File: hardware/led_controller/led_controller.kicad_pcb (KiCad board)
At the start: 2 copper layers, 50 x 70 mm, 31 parts, among them J1 Header, J2 Header, J3 Header, J4 Header, J5 POWER, J6 Conn_01x02, U1 74AHCT125, U3 Waveshare ESP32-S3/C6 Zero

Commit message: Updated footprint
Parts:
- J6: footprint TerminalBlock_Phoenix:TerminalBlock_Phoenix_MPT-0,5-2-2.54_1x02_P2.54mm_Horizontal -> TerminalBlock:TerminalBlock_Xinya_XY308-2.54-2P_1x02_P2.54mm_Horizontal
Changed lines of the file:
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@@
 		)
 	)
-	(footprint "TerminalBlock_Phoenix:TerminalBlock_Phoenix_MPT-0,5-2-2.54_1x02_P2.54mm_Horizontal"
+	(footprint "TerminalBlock:TerminalBlock_Xinya_XY308-2.54-2P_1x02_P2.54mm_Horizontal"
 		(layer "F.Cu")
 		(at 162.2175 95.975 90)
-		(descr "Terminal Block Phoenix MPT-0,5-2-2.54, 2 pins, pitch 2.54mm, size 5.54x6.2mm, drill diameter 1.1mm, pad diameter 2.2mm, http://www.mouser.com/ds/2/324/ItemDetail_1725656-920552.pdf")
-		(tags "THT Terminal Block Phoenix MPT-0,5-2-2.54 pitch 2.54mm size 5.54x6.2mm drill 1.1mm pad 2.2mm")
+		(descr "Terminal Block Xinya XY308-2.54-2P, 2 pins, pitch 2.54mm, size 5.58x6.5mm, drill diameter 1.2mm, pad diameter 2mm, http://www.xinyaelectronic.com/product/xy308-254")
+		(tags "THT Terminal Block Xinya XY308-2.54-2P pitch 2.54mm size 5.58x6.5mm drill 1.2mm pad 2mm")
 		(property "Reference" "J6"
-			(at -3.025 -0.0175 180)
+			(at -2.925 0.1825 180)
 			(layer "F.SilkS")
 			(effects
@@
 		)
 		(property "Value" "Conn_01x02"
-			(at 1.27 4.22 90)
+			(at 1.27 4.52 90)
 			(layer "F.Fab")
 			(effects
@@
 		(duplicate_pad_numbers_are_jumpers no)
 		(fp_line
-			(start 4.16 -3.22)
-			(end 4.16 3.22)
+			(start 4.18 -3.22)
+			(end 4.18 3.52)
 			(stroke
 				(width 0.12)
@@
 		)
 		(fp_line
-			(start -1.62 -3.22)
-			(end 4.16 -3.22)
+			(start -1.64 -3.22)
+			(end 4.18 -3.22)
 			(stroke
 				(width 0.12)
@@
 		)
 		(fp_line
-			(start -1.62 -2.7)
-			(end 4.16 -2.7)
+			(start -1.64 -1.5)
+			(end 4.18 -1.5)
 			(stroke
 				(width 0.12)
@@
 		)
 		(fp_line
-			(start 3.57 2.6)
-			(end 4.16 2.6)
+			(start -1.64 1.6)
+			(end 4.18 1.6)
 			(stroke
 				(width 0.12)
@@
 		)
 		(fp_line
-			(start 1.03 2.6)
-			(end 1.51 2.6)
+			(start -1.64 2.6)
+			(end 4.18 2.6)
 			(stroke
 				(width 0.12)
@@
 		)
 		(fp_line
-			(start -1.62 2.6)
-			(end -1.03 2.6)
+			(start 4.18 3.52)
+			(end 0.3 3.52)
 			(stroke
 				(width 0.12)
@@
 		)
 		(fp_line
-			(start 4.16 3.22)
-			(end 3.57 3.22)
+			(start -0.3 3.52)
+			(end -1.64 3.52)
 			(stroke
 				(width 0.12)
@@
 		)
 		(fp_line
-			(start 1.51 3.22)
-			(end 1.03 3.22)
-			(stroke
-				(width 0.12)
-				(type solid)
-			)
-			(layer "F.SilkS")
-		)
-		(fp_line
-			(start -1.03 3.22)
-			(end -1.62 3.22)
-			(stroke
-				(width 0.12)
-				(type solid)
-			)
-			(layer "F.SilkS")
-		)
-		(fp_line
-			(start -1.62 3.22)
-			(end -1.62 -3.22)
+			(start -1.64 3.52)
+			(end -1.64 -3.22)
 			(stroke
 				(width 0.12)
@@
 		(fp_poly
 			(pts
-				(xy 0 3.57) (xy 0.44 4.18) (xy -0.44 4.18)
+				(xy 0 3.52) (xy 0.44 4.13) (xy -0.44 4.13)
 			)
 			(stroke
@@
 		)
 		(fp_rect
-			(start -2 -3.6)
-			(end 4.54 3.6)
+			(start -2.02 -3.6)
+			(end 4.57 3.9)
 			(stroke
 				(width 0.05)
@@
 		)
 		(fp_line
-			(start 4.04 -3.1)
-			(end 4.04 3.1)
+			(start 4.06 -3.1)
+			(end 4.06 3.4)
 			(stroke
 				(width 0.1)
@@
 		)
 		(fp_line
-			(start -1.5 -3.1)
-			(end 4.04 -3.1)
+			(start -1.52 -3.1)
+			(end 4.06 -3.1)
 			(stroke
 				(width 0.1)
@@
 		)
 		(fp_line
-			(start -1.5 -2.7)
-			(end 4.04 -2.7)
+			(start -1.52 -1.5)
+			(end 4.06 -1.5)
 			(stroke
 				(width 0.1)
@@
 		)
 		(fp_line
-			(start 3.24 -0.834)
-			(end 1.706 0.7)
+			(start 3.176 -0.758)
+			(end 1.782 0.636)
 			(stroke
 				(width 0.1)
@@
 		)
 		(fp_line
-			(start 0.7 -0.834)
-			(end -0.834 0.7)
+			(start 0.636 -0.758)
+			(end -0.758 0.636)
 			(stroke
 				(width 0.1)
@@
 		)
 		(fp_line
-			(start 3.374 -0.7)
-			(end 1.84 0.834)
+			(start 3.298 -0.636)
+			(end 1.904 0.758)
 			(stroke
 				(width 0.1)
@@
 		)
 		(fp_line
-			(start 0.834 -0.7)
-			(end -0.7 0.834)
+			(start 0.758 -0.636)
+			(end -0.636 0.758)
 			(stroke
 				(width 0.1)
@@
 		)
 		(fp_line
-			(start -1.5 2.6)
-			(end -1.5 -3.1)
+			(start -1.52 1.6)
+			(end 4.06 1.6)
 			(stroke
 				(width 0.1)
@@
 		)
 		(fp_line
-			(start -1.5 2.6)
-			(end 4.04 2.6)
+			(start -1.52 2.6)
+			(end -1.52 -3.1)
 			(stroke
 				(width 0.1)
@@
 		)
 		(fp_line
-			(start 4.04 3.1)
-			(end -1 3.1)
+			(start -1.52 2.6)
+			(end 4.06 2.6)
 			(stroke
 				(width 0.1)
@@
 		)
 		(fp_line
-			(start -1 3.1)
-			(end -1.5 2.6)
+			(start 4.06 3.4)
+			(end -0.72 3.4)
+			(stroke
+				(width 0.1)
+				(type solid)
+			)
+			(layer "F.Fab")
+		)
+		(fp_line
+			(start -0.72 3.4)
+			(end -1.52 2.6)
 			(stroke
 				(width 0.1)
@@
 		(fp_circle
 			(center 2.54 0)
-			(end 3.64 0)
+			(end 3.54 0)
 			(stroke
 				(width 0.1)
@@
 		(fp_circle
 			(center 0 0)
-			(end 1.1 0)
+			(end 1 0)
 			(stroke
 				(width 0.1)
@@
 		)
 		(fp_text user "${REFERENCE}"
-			(at 1.27 2 90)
+			(at 1.27 2.15 90)
 			(layer "F.Fab")
 			(effects
@@
 			)
 		)
-		(pad "" np_thru_hole circle
-			(at 0 2.54 90)
-			(size 1.1 1.1)
-			(drill 1.1)
-			(layers "*.Cu" "*.Mask")
-		)
-		(pad "" np_thru_hole circle
-			(at 2.54 2.54 90)
-			(size 1.1 1.1)
-			(drill 1.1)
-			(layers "*.Cu" "*.Mask")
-		)
 		(pad "1" thru_hole roundrect
 			(at 0 0 90)
-			(size 2.2 2.2)
-			(drill 1.1)
+			(size 2 2)
+			(drill 1.2)
 			(layers "*.Cu" "*.Mask")
 			(remove_unused_layers no)
-			(roundrect_rratio 0.113636)
+			(roundrect_rratio 0.125)
 			(net "GND")
 			(pinfunction "Pin_1_1")
@@
 		(pad "2" thru_hole circle
 			(at 2.54 0 90)
-			(size 2.2 2.2)
-			(drill 1.1)
+			(size 2 2)
+			(drill 1.2)
 			(layers "*.Cu" "*.Mask")
 			(remove_unused_layers no)
@@
 		)
 		(embedded_fonts no)
-		(model "${KICAD10_3DMODEL_DIR}/TerminalBlock_Phoenix.3dshapes/TerminalBlock_Phoenix_MPT-0,5-2-2.54_1x02_P2.54mm_Horizontal.step"
+		(model "${KICAD10_3DMODEL_DIR}/TerminalBlock.3dshapes/TerminalBlock_Xinya_XY308-2.54-2P_1x02_P2.54mm_Horizontal.step"
 			(offset
 				(xyz 0 0 0)
@@
 		(tags "capacitor handsolder")
 		(property "Reference" "C9"
-			(at 0 -1.85 0)
+			(at -0.2 1.9 0)
 			(layer "F.SilkS")
 			(effects

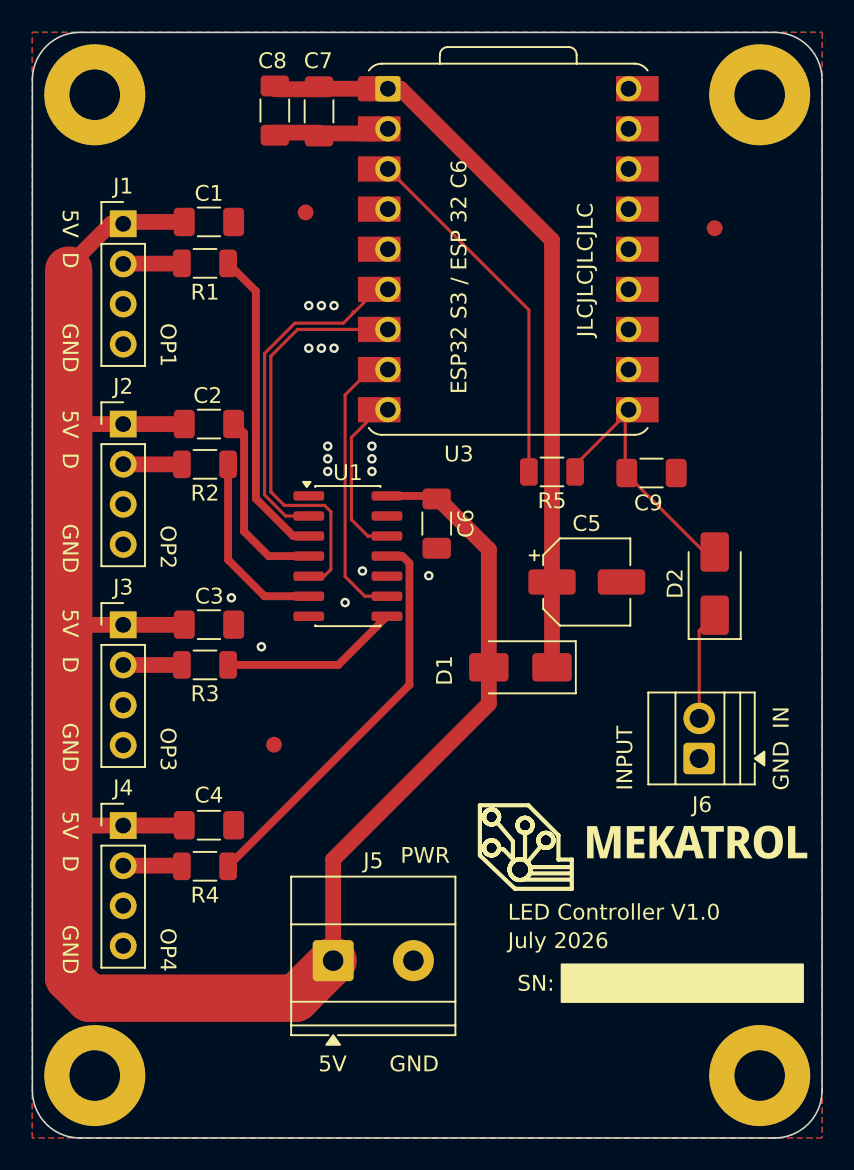
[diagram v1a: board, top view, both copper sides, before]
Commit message: Update hole layout
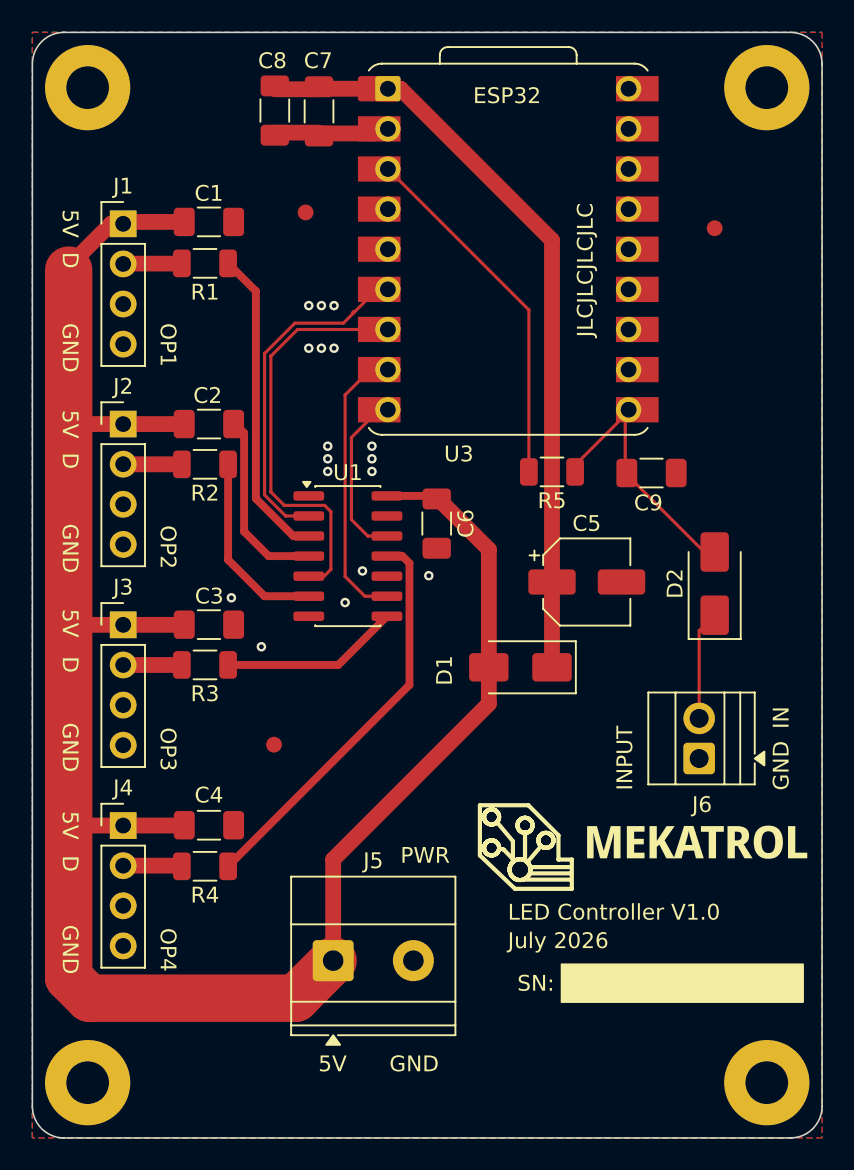
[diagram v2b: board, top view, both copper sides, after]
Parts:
- H1, H2, H3, H4: footprint MountingHole:MountingHole_3.2mm_M3_Pad -> MountingHole:MountingHole_2.7mm_M2.5_Pad
- moved H1 0.64 mm to (123.5, 53.5)
- moved H3 0.64 mm to (123.5, 116.5)
- moved H2 0.64 mm to (166.5, 53.5)
- moved H4 0.64 mm to (166.5, 116.5)
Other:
- outline, holes or cut-outs redrawn
- board text added: "ESP32"
- board text removed: "ESP32 S3 / ESP 32 C6"
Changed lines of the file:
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@@
 		)
 	)
-	(footprint "MountingHole:MountingHole_3.2mm_M3_Pad"
+	(footprint "MountingHole:MountingHole_2.7mm_M2.5_Pad"
 		(layer "F.Cu")
-		(at 166.05 116.05)
-		(descr "Mounting Hole 3.2mm, M3, generated by kicad-footprint-generator mountinghole.py")
-		(tags "mountinghole M3")
+		(at 166.5 116.5)
+		(descr "Mounting Hole 2.7mm, M2.5, generated by kicad-footprint-generator mountinghole.py")
+		(tags "mountinghole M2.5")
 		(property "Reference" "H4"
-			(at 0 -4.15 0)
+			(at 0 -3.65 0)
 			(layer "F.SilkS")
 			(hide yes)
@@
 		)
 		(property "Value" "MountingHole_Pad"
-			(at 0 4.15 0)
+			(at 0 3.65 0)
 			(layer "F.Fab")
 			(hide yes)
@@
 		(fp_circle
 			(center 0 0)
-			(end 3.2 0)
+			(end 2.7 0)
 			(stroke
 				(width 0.15)
@@
 		(fp_circle
 			(center 0 0)
-			(end 3.45 0)
+			(end 2.95 0)
 			(stroke
 				(width 0.05)
@@
 		(pad "1" thru_hole circle
 			(at 0 0)
-			(size 6.4 6.4)
-			(drill 3.2)
+			(size 5.4 5.4)
+			(drill 2.7)
 			(layers "*.Cu" "*.Mask")
 			(remove_unused_layers no)
@@
 		)
 	)
-	(footprint "MountingHole:MountingHole_3.2mm_M3_Pad"
+	(footprint "MountingHole:MountingHole_2.7mm_M2.5_Pad"
 		(layer "F.Cu")
-		(at 166.05 53.95)
-		(descr "Mounting Hole 3.2mm, M3, generated by kicad-footprint-generator mountinghole.py")
-		(tags "mountinghole M3")
+		(at 166.5 53.5)
+		(descr "Mounting Hole 2.7mm, M2.5, generated by kicad-footprint-generator mountinghole.py")
+		(tags "mountinghole M2.5")
 		(property "Reference" "H2"
-			(at 0 -4.15 0)
+			(at 0 -3.65 0)
 			(layer "F.SilkS")
 			(hide yes)
@@
 		)
 		(property "Value" "MountingHole_Pad"
-			(at 0 4.15 0)
+			(at 0 3.65 0)
 			(layer "F.Fab")
 			(hide yes)
@@
 		(fp_circle
 			(center 0 0)
-			(end 3.2 0)
+			(end 2.7 0)
 			(stroke
 				(width 0.15)
@@
 		(fp_circle
 			(center 0 0)
-			(end 3.45 0)
+			(end 2.95 0)
 			(stroke
 				(width 0.05)
@@
 		(pad "1" thru_hole circle
 			(at 0 0)
-			(size 6.4 6.4)
-			(drill 3.2)
+			(size 5.4 5.4)
+			(drill 2.7)
 			(layers "*.Cu" "*.Mask")
 			(remove_unused_layers no)
@@
 		)
 	)
-	(footprint "MountingHole:MountingHole_3.2mm_M3_Pad"
+	(footprint "MountingHole:MountingHole_2.7mm_M2.5_Pad"
 		(layer "F.Cu")
-		(at 123.95 53.95)
-		(descr "Mounting Hole 3.2mm, M3, generated by kicad-footprint-generator mountinghole.py")
-		(tags "mountinghole M3")
+		(at 123.5 53.5)
+		(descr "Mounting Hole 2.7mm, M2.5, generated by kicad-footprint-generator mountinghole.py")
+		(tags "mountinghole M2.5")
 		(property "Reference" "H1"
-			(at 4.65 0.05 0)
+			(at 0 -3.65 0)
 			(layer "F.SilkS")
 			(hide yes)
@@
 		)
 		(property "Value" "MountingHole_Pad"
-			(at 0 4.15 0)
+			(at 0 3.65 0)
 			(layer "F.Fab")
 			(hide yes)
@@
 		(fp_circle
 			(center 0 0)
-			(end 3.2 0)
+			(end 2.7 0)
 			(stroke
 				(width 0.15)
@@
 		(fp_circle
 			(center 0 0)
-			(end 3.45 0)
+			(end 2.95 0)
 			(stroke
 				(width 0.05)
@@
 		(pad "1" thru_hole circle
 			(at 0 0)
-			(size 6.4 6.4)
-			(drill 3.2)
+			(size 5.4 5.4)
+			(drill 2.7)
 			(layers "*.Cu" "*.Mask")
 			(remove_unused_layers no)
@@
 		(embedded_fonts no)
 	)
-	(footprint "MountingHole:MountingHole_3.2mm_M3_Pad"
+	(footprint "MountingHole:MountingHole_2.7mm_M2.5_Pad"
 		(layer "F.Cu")
-		(at 123.95 116.05)
-		(descr "Mounting Hole 3.2mm, M3, generated by kicad-footprint-generator mountinghole.py")
-		(tags "mountinghole M3")
+		(at 123.5 116.5)
+		(descr "Mounting Hole 2.7mm, M2.5, generated by kicad-footprint-generator mountinghole.py")
+		(tags "mountinghole M2.5")
 		(property "Reference" "H3"
-			(at 0 -4.15 0)
+			(at 0 -3.65 0)
 			(layer "F.SilkS")
 			(hide yes)
@@
 		)
 		(property "Value" "MountingHole_Pad"
-			(at 0 4.15 0)
+			(at 0 3.65 0)
 			(layer "F.Fab")
 			(hide yes)
@@
 		(fp_circle
 			(center 0 0)
-			(end 3.2 0)
+			(end 2.7 0)
 			(stroke
 				(width 0.15)
@@
 		(fp_circle
 			(center 0 0)
-			(end 3.45 0)
+			(end 2.95 0)
 			(stroke
 				(width 0.05)
@@
 		(pad "1" thru_hole circle
 			(at 0 0)
-			(size 6.4 6.4)
-			(drill 3.2)
+			(size 5.4 5.4)
+			(drill 2.7)
 			(layers "*.Cu" "*.Mask")
 			(remove_unused_layers no)
@@
 	)
 	(gr_arc
-		(start 120 53)
-		(mid 120.878679 50.878679)
-		(end 123 50)
+		(start 120 52)
+		(mid 120.585786 50.585786)
+		(end 122 50)
 		(stroke
 			(width 0.1)
@@
 	)
 	(gr_line
-		(start 120 117)
-		(end 120 53)
+		(start 120 118)
+		(end 120 52)
 		(stroke
 			(width 0.1)
@@
 	)
 	(gr_line
-		(start 123 50)
-		(end 167 50)
+		(start 122 50)
+		(end 168 50)
 		(stroke
 			(width 0.1)
@@
 	)
 	(gr_arc
-		(start 123 120)
-		(mid 120.878679 119.12132)
-		(end 120 117)
+		(start 122 120)
+		(mid 120.585786 119.414213)
+		(end 120 118)
 		(stroke
 			(width 0.1)
@@
 	)
 	(gr_arc
-		(start 167 50)
-		(mid 169.12132 50.878679)
-		(end 170 53)
+		(start 168 50)
+		(mid 169.414213 50.585786)
+		(end 170 52)
 		(stroke
 			(width 0.1)
@@
 	)
 	(gr_line
-		(start 167 120)
-		(end 123 120)
+		(start 168 120)
+		(end 122 120)
 		(stroke
 			(width 0.1)
@@
 	)
 	(gr_line
-		(start 170 53)
-		(end 170 117)
+		(start 170 52)
+		(end 170 118)
 		(stroke
 			(width 0.1)
@@
 	)
 	(gr_arc
-		(start 170 117)
-		(mid 169.12132 119.12132)
-		(end 167 120)
+		(start 170 118)
+		(mid 169.414213 119.414213)
+		(end 168 120)
 		(stroke
 			(width 0.1)
@@
 		)
 	)
-	(gr_text "SN:"
-		(at 150.7 110.8 0)
+	(gr_text "ESP32"
+		(at 147.9 54.6 0)
 		(layer "F.SilkS")
 		(effects
@@
 		)
 	)
-	(gr_text "ESP32 S3 / ESP 32 C6"
-		(at 147.6 72.9 90)
+	(gr_text "SN:"
+		(at 150.7 110.8 0)
 		(layer "F.SilkS")
 		(effects

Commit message: Update PCB, generate gerber does fill zone and DRC checks
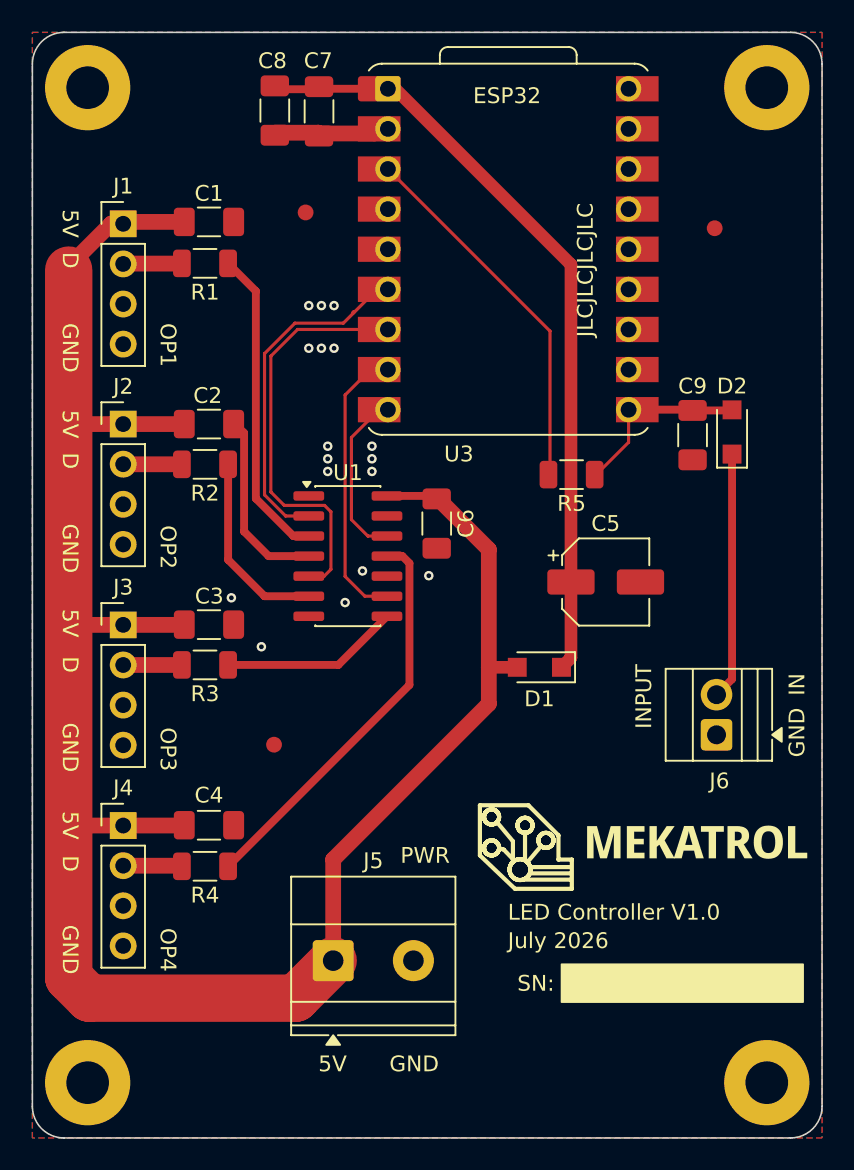
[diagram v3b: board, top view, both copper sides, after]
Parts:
- D1, D2: footprint Diode_SMD:D_SMA -> Diode_SMD:Nexperia_CFP3_SOD-123W
- moved D2 9.66 mm to (164.3, 75.3)
- moved C9 3.54 mm to (161.8, 75.5), turned to -90 degrees
- moved J6 1.86 mm to (163.3, 94.5)
- moved R5 1.25 mm to (154.1, 78.0)
- moved C5 1.20 mm to (156.3, 84.8)
- moved D1 1.20 mm to (152.1, 90.2)
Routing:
- net Net-(D2-K): track 6.94 -> 15.6 mm
- net Net-(D2-A): track 17.5 -> 11.0 mm
- net +5V: track 131.7 -> 133.5 mm
- net +3.3V: track 22.4 -> 23.6 mm
- net +4.6V: track 48.6 -> 49.1 mm
